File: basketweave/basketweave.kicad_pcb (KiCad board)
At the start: 2 copper layers, 371.5 x 145.3 mm, 177 parts, among them U1 ATmega32A-PU, Y1 16Mhz

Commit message: Move macro keys to the right and encoder to the left
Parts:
- removed G***: LOGO, basketweave:logo
- removed MX16, MX31: MX-NoLED, MX_Only:MXOnly-1U-NoLED
- removed REF**: pattern_right, basketweave:pattern_right
- removed REF**: pattern_left, basketweave:pattern_left
- removed ROTARY ENCODER: Rotary_Encoder_Switch, Rotary_Encoder:RotaryEncoder_Alps_EC11E-Switch_Vertical_H20mm
- added D73: D_Small, Diode_THT:D_DO-35_SOD27_P7.62mm_Horizontal, F.Cu at (371.6, 143.3)
- added D74: D_Small, Diode_THT:D_DO-35_SOD27_P7.62mm_Horizontal, F.Cu at (376.4, 162.3)
- added MX72: MX-NoLED, MX_Only:MXOnly-1U-NoLED, F.Cu at (370.7, 115.9)
- added MX73: MX-NoLED, MX_Only:MXOnly-1U-NoLED, F.Cu at (375.4, 134.9)
- added MX74: MX-NoLED, MX_Only:MXOnly-1U-NoLED, F.Cu at (380.2, 154.0)
- added SW3: Rotary_Encoder_Switch, Rotary_Encoder:RotaryEncoder_Alps_EC11E-Switch_Vertical_H20mm, F.Cu at (31.0, 153.9)
- moved D72 10.1 mm to (366.8, 124.2)
- renumbered POWER to D71, ISP to J1, BOOT to SW1, RESET to SW2, USB to U2
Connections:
- D16 pad 2: Net-(D16-Pad2) -> (no net)
- D72 pad 1: ROW4 -> ROW0
- MX30 pad 1: COL14 -> Net-(MX30-Pad1)
- MX59 pad 1: COL14 -> Net-(MX30-Pad1)
- MX62 pad 2: Net-(D61-Pad2) -> (no net)
- MX63 pad 2: Net-(D62-Pad2) -> (no net)
- MX69 pad 1: COL14 -> Net-(MX30-Pad1)
- U1 pad 14: Net-(U1-Pad14) -> (no net)
- U1 pad 15: Net-(U1-Pad15) -> (no net)
- U1 pad 21: EN1 -> (no net)
- U1 pad 22: EN2 -> COL15
- U1 pad 32: Net-(U1-Pad32) -> (no net)
- U1 pad 4: Net-(U1-Pad4) -> EN1
- U1 pad 5: Net-(U1-Pad5) -> EN2
- U2 pad A8: Net-(U2-PadA8) -> (no net)
- U2 pad B1: GND -> Net-(U2-PadB1)
- U2 pad B8: Net-(U2-PadB8) -> (no net)
- U2 pad S1: GND -> Net-(U2-PadB1)
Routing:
- net COL15: track 0.00 -> 197.0 mm
- net COL14: track 290.5 -> 147.1 mm
- net ROW2: track 436.5 -> 528.9 mm
- net ROW1: track 430.9 -> 514.5 mm, vias 4 -> 3
- net Net-(MX30-Pad1): track 0.00 -> 80.2 mm
- net ROW0: track 382.1 -> 458.2 mm
- net EN2: track 166.0 -> 236.1 mm
- net EN1: track 161.3 -> 226.7 mm
- net Net-(D16-Pad2): track 43.3 -> 0.00 mm
- net ROW4: track 453.7 -> 425.5 mm
- net Net-(D74-Pad2): track 0.00 -> 13.9 mm
- net Net-(D73-Pad2): track 0.00 -> 13.9 mm
- net Net-(D72-Pad2): track 7.47 -> 13.9 mm
- net Net-(D31-Pad2): track 59.1 -> 64.8 mm
- net Net-(D59-Pad2): track 101.9 -> 97.6 mm
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
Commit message: Make macro keys symmetric on both sides; move encoder to the left
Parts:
- added MX16: MX-NoLED, MX_Only:MXOnly-1U-NoLED, F.Cu at (42.1, 134.9)
- added MX75: MX-NoLED, MX_Only:MXOnly-1U-NoLED, F.Cu at (37.3, 154.0)
- moved SW3 11.5 mm to (39.8, 146.5), turned to 270 degrees
- moved D72 2.61 mm to (369.1, 125.3)
- moved D73 2.56 mm to (373.9, 144.4)
- moved D74 2.56 mm to (378.7, 163.4)
- moved H2 1.13 mm to (29.4, 101.6)
- moved H4 1.13 mm to (392.9, 101.6)
- moved H5 0.83 mm to (164.2, 101.6)
- moved H6 0.83 mm to (234.2, 101.6)
- moved H1 0.76 mm to (29.4, 84.2)
- moved H3 0.76 mm to (392.9, 84.2)
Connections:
- D16 pad 2: (no net) -> Net-(D16-Pad2)
- U2 pad B1: Net-(U2-PadB1) -> GND
- U2 pad S1: Net-(U2-PadB1) -> GND
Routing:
- net GND: track 97.3 -> 26.2 mm, vias 7 -> 8
- net Net-(D16-Pad2): track 0.00 -> 41.1 mm
- net EN2: track 236.1 -> 221.7 mm
- net Net-(D31-Pad2): track 64.8 -> 73.5 mm
- net COL0: track 186.6 -> 193.1 mm
- net EN1: track 226.7 -> 222.8 mm
- net ROW1: track 514.5 -> 517.9 mm
- net ROW2: track 528.9 -> 532.2 mm
- net ROW0: track 458.2 -> 461.3 mm
- net Net-(D72-Pad2): track 13.9 -> 16.0 mm
- net Net-(D74-Pad2): track 13.9 -> 16.0 mm
- net Net-(D73-Pad2): track 13.9 -> 16.0 mm
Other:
- board text added: "Basketweave-S"
- board text added: "MX/Encoder"
- board text added: "Modified by piit79"
- board text added: "Rev 1.5"
- board text added: "github.com/piit79/basketweave-s"
- board text removed: "Rev 1"

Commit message: Add back PCB patterns above diodes
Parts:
- added PATTERN1: Pattern_Left, basketweave:pattern_left, F.Cu at (39.7, 86.5)
- added PATTERN2: Pattern_Right, basketweave:pattern_right, F.Cu at (253.2, 86.5)

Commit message: Add second rotary encoder on the right
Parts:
- added SW4: Rotary_Encoder_Switch, basketweave:RotaryEncoder_Alps_EC11E-Switch_Vertical_H20mm-for-MX, F.Cu at (382.7, 146.5)
- SW1: value SW_Push -> BOOT
- SW2: value SW_Push -> RESET
- SW3: footprint Rotary_Encoder:RotaryEncoder_Alps_EC11E-Switch_Vertical_H20mm -> basketweave:RotaryEncoder_Alps_EC11E-Switch_Vertical_H20mm-for-MX
- moved D73 0.70 mm to (373.9, 143.7)
- moved D74 0.38 mm to (378.7, 163.8)
- renumbered U2 to USB1
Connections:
- net EN1 renamed EN_A1
- net EN2 renamed EN_A2
- MX30 pad 1: Net-(MX30-Pad1) -> COL14
- MX59 pad 1: Net-(MX30-Pad1) -> COL14
- MX62 pad 2: (no net) -> Net-(D61-Pad2)
- MX63 pad 2: (no net) -> Net-(D62-Pad2)
- MX69 pad 1: Net-(MX30-Pad1) -> COL14
- U1 pad 14: (no net) -> EN_B2
- U1 pad 15: (no net) -> EN_B1
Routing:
- net EN_B1: track 0.00 -> 275.6 mm
- net EN_B2: track 0.00 -> 271.1 mm
- net Net-(MX30-Pad1): track 80.2 -> 0.00 mm
- net COL14: track 147.1 -> 227.3 mm
- net COL15: track 197.0 -> 207.1 mm
- net ROW4: track 425.5 -> 423.3 mm
- net Net-(D74-Pad2): track 16.0 -> 16.9 mm
- net Net-(D73-Pad2): track 16.0 -> 15.3 mm
- net Net-(D62-Pad2): track 224.7 -> 225.3 mm
- net COL6: track 108.5 -> 109.1 mm
- net Net-(D61-Pad2): track 199.4 -> 200.0 mm
- net COL4: track 162.7 -> 163.2 mm
- net GND: vias 8 -> 10
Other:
- board text added: "Rev 1.6"
- board text removed: "Rev 1.5"

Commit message: Add support for encoders in the top macro positions
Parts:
- added SW5: Rotary_Encoder_Switch, basketweave:RotaryEncoder_Alps_EC11E-Switch_Vertical_H20mm-for-MX, F.Cu at (49.3, 108.4)
- added SW6: Rotary_Encoder_Switch, basketweave:RotaryEncoder_Alps_EC11E-Switch_Vertical_H20mm-for-MX, F.Cu at (373.2, 108.4)
- moved D66 3.55 mm to (370.7, 93.7)
- moved D68 3.55 mm to (367.5, 95.3)
- moved D72 0.25 mm to (369.1, 125.6)
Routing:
- net EN_A1: track 222.8 -> 238.6 mm
- net Net-(D1-Pad2): track 9.65 -> 23.5 mm
- net EN_A2: track 221.7 -> 231.8 mm
- net EN_B1: track 275.6 -> 267.6 mm
- net Net-(D59-Pad2): track 97.6 -> 103.2 mm
- net Net-(D31-Pad2): track 73.5 -> 79.1 mm
- net EN_B2: track 271.1 -> 266.4 mm
- net Net-(D66-Pad2): track 118.5 -> 122.8 mm
- net Net-(D68-Pad2): track 142.1 -> 138.3 mm
- net Net-(D16-Pad2): track 41.1 -> 44.7 mm
- net ROW3: track 383.2 -> 380.6 mm
- net ROW4: track 423.3 -> 425.6 mm
- net Net-(D72-Pad2): track 16.0 -> 18.2 mm
- net COL0: track 193.1 -> 194.2 mm
- net ROW2: track 531.8 -> 532.7 mm
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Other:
- board text added: "Based on Basketweave by Noah L github.com/null-ll/basketweave"
- board text added: "JLCJLCJLCJLC"
- board text added: "MX/Encoder1"
- board text added: "MX/Encoder2"
- board text added: "Modified by piit79 of 42keebs.eu github.com/piit79/basketweave-s"
- board text added: "Rev 1.8"
- board text removed: "Designed by Noah L"
- board text removed: "MX/Encoder"
- board text removed: "Modified by piit79"
- board text removed: "Rev 1.6"
- board text removed: "github.com/null-ll/basketweave"
- board text removed: "github.com/piit79/basketweave-s"

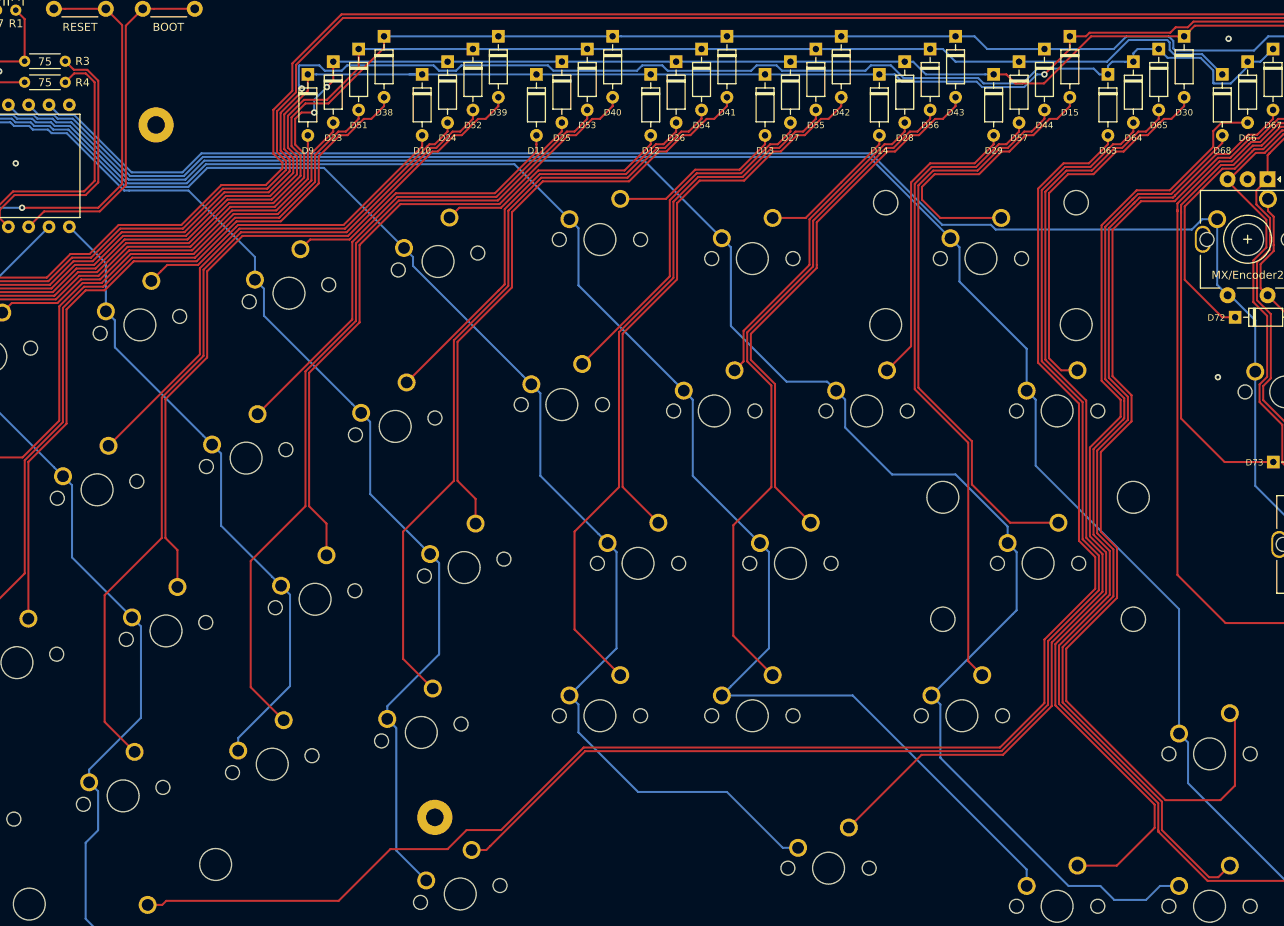
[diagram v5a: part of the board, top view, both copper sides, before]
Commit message: Add support for split backspace
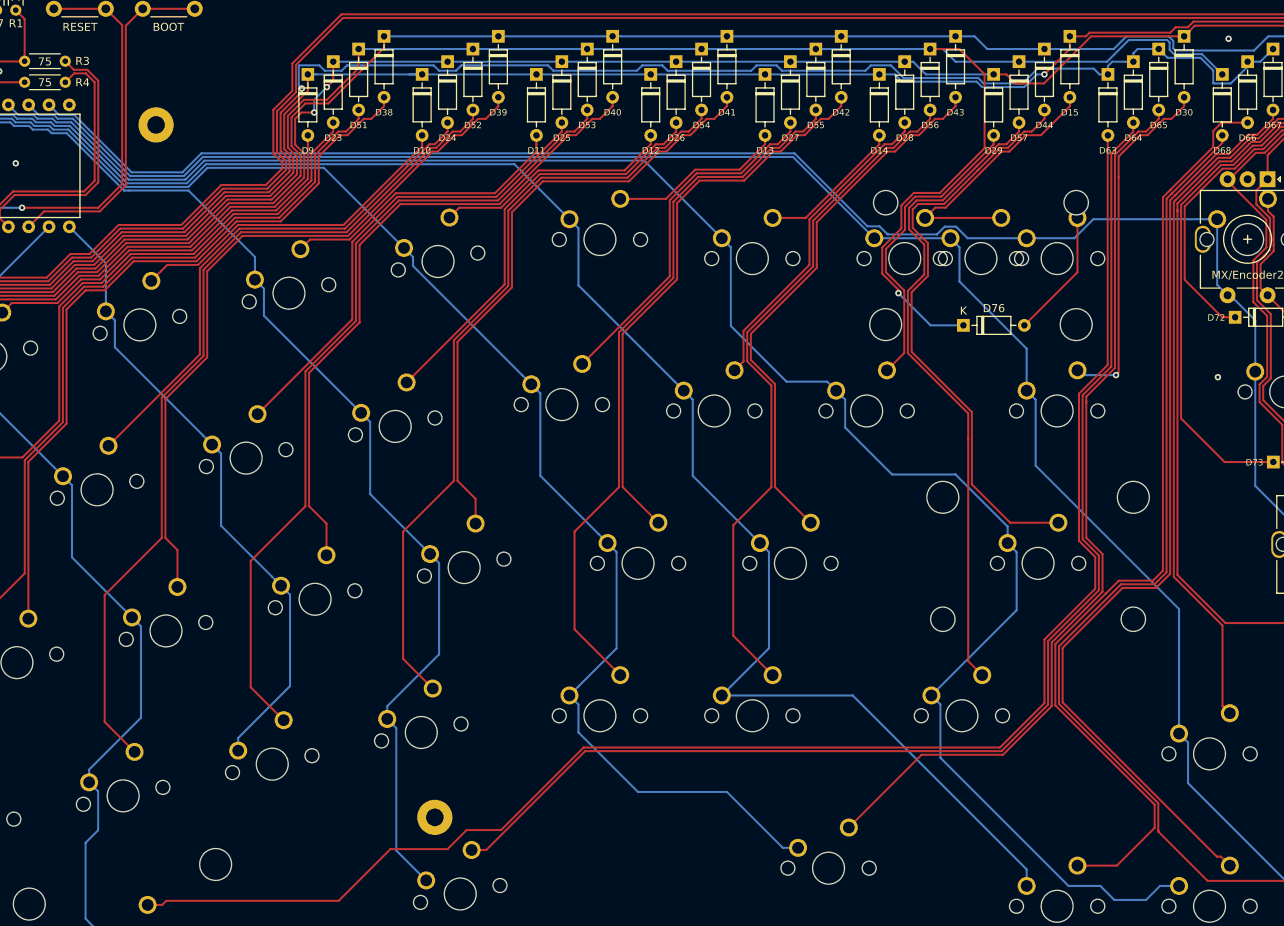
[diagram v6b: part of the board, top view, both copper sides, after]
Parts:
- added D76: D_Small, Diode_THT:D_DO-35_SOD27_P7.62mm_Horizontal, F.Cu at (335.2, 126.6)
- added MX31: MX-NoLED, MX_Only:MXOnly-1U-NoLED, F.Cu at (327.8, 118.3)
- added MX76: MX-NoLED, MX_Only:MXOnly-1U-NoLED, F.Cu at (346.9, 118.3)
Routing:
- net ROW3: track 380.6 -> 434.0 mm, vias 1 -> 2
- net Net-(D58-Pad2): track 132.0 -> 88.6 mm
- net Net-(D76-Pad2): track 0.00 -> 16.2 mm
- net Net-(D67-Pad2): track 125.5 -> 118.4 mm
- net Net-(D64-Pad2): track 165.1 -> 158.4 mm
- net Net-(D65-Pad2): track 120.6 -> 114.2 mm
- net Net-(D63-Pad2): track 205.1 -> 199.0 mm
- net Net-(D68-Pad2): track 138.3 -> 134.6 mm
- net Net-(D66-Pad2): track 122.8 -> 119.4 mm
- net Net-(D30-Pad2): track 47.3 -> 44.8 mm, vias 0 -> 1
- net COL15: track 207.3 -> 209.0 mm
- net Net-(D15-Pad2): track 36.2 -> 34.5 mm
- net Net-(D57-Pad2): track 81.8 -> 83.2 mm
- net Net-(D44-Pad2): track 73.3 -> 74.3 mm
- net Net-(D29-Pad2): track 38.1 -> 38.7 mm
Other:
- board text added: "Rev 1.9"
- board text removed: "Rev 1.8"
